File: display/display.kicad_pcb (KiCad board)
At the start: 2 copper layers, 68.4 x 20.5 mm, 46 parts, among them P1 CONN_14

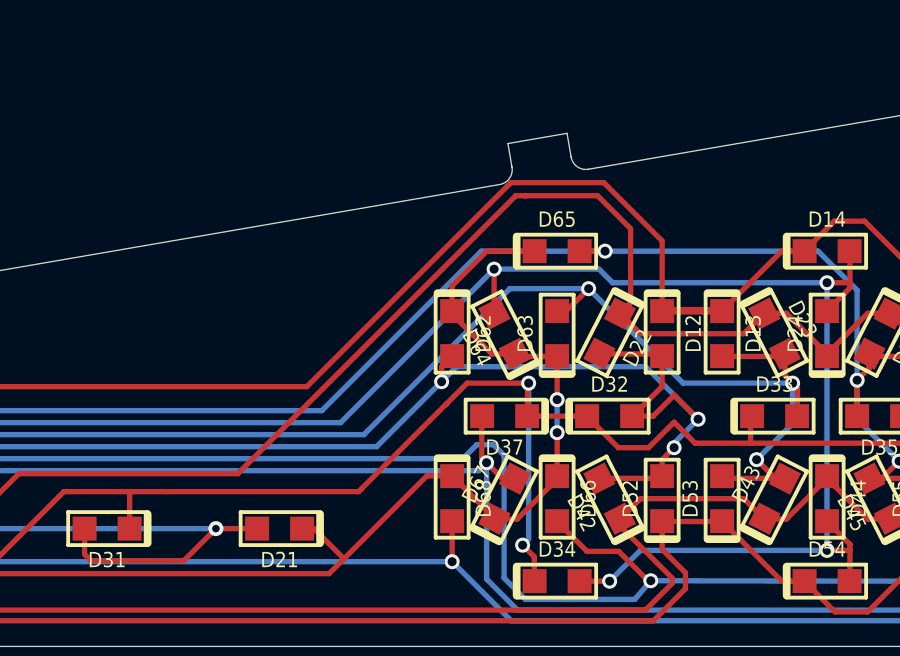
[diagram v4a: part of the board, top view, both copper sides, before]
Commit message: Route tracks farther from the contour.
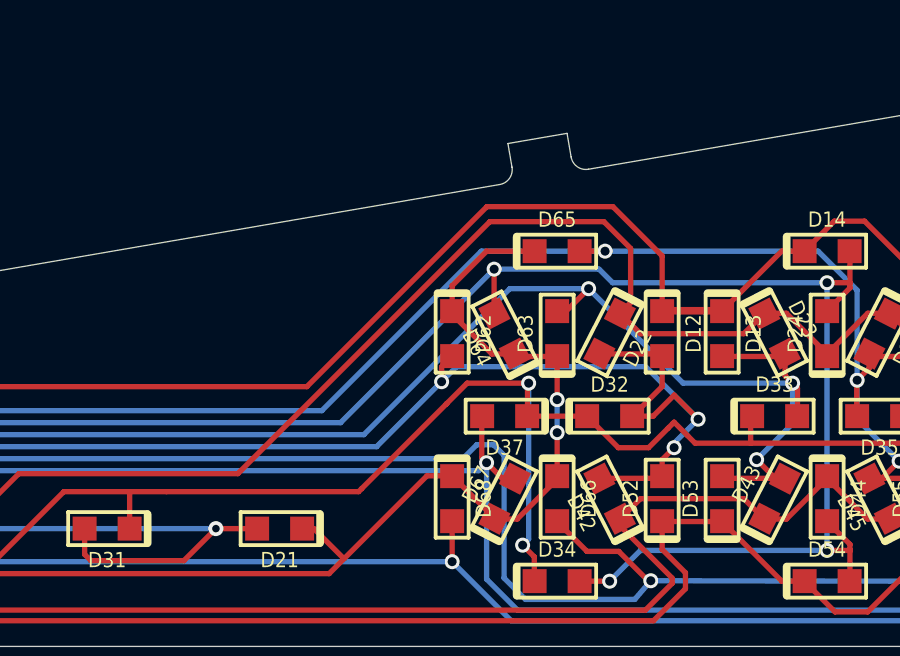
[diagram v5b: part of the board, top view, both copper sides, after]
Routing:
- net (no net): track 0.00 -> 57.8 mm
- net /ROW2: track 60.9 -> 18.8 mm
- net /ROW1: track 63.4 -> 45.6 mm
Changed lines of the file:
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@@
     (thickness 1.6002)
     (drawings 33)
-    (tracks 382)
+    (tracks 379)
     (zones 0)
     (modules 46)
@@
   (gr_line (start 135.992156 96.388669) (end 136.127883 97.177067) (angle 90) (layer Edge.Cuts) (width 0.01))
   (gr_arc (start 135.635143 97.2619) (end 135.719962 97.754651) (angle -90.01309679) (layer Edge.Cuts) (width 0.01))
+  (segment (start 160.84296 98.58178) (end 160.84296 96.74296) (width 0.1778) (layer Front) (net 0) (status 400000))
+  (segment (start 131.419099 101.1) (end 149 101.1) (width 0.1778) (layer Front) (net 9) (status 1000000))
+  (segment (start 131.419099 101.1) (end 130.402749 102.11635) (width 0.1778) (layer Front) (net 9) (status 1000000))
+  (segment (start 155 95.1) (end 149 101.1) (width 0.1778) (layer Front) (net 0) (status 1000000))
+  (segment (start 159.2 95.1) (end 155 95.1) (width 0.1778) (layer Front) (net 0) (status 1000000))
+  (segment (start 160.84296 96.74296) (end 159.2 95.1) (width 0.1778) (layer Front) (net 0) (status 1000000))
+  (segment (start 159.7914 98.30308) (end 159.7914 96.4914) (width 0.1778) (layer Front) (net 0))
+  (segment (start 146.7 104) (end 139.39936 104) (width 0.1778) (layer Front) (net 10))
+  (segment (start 139.39936 104) (end 137.56772 105.83164) (width 0.1778) (layer Front) (net 10))
+  (segment (start 174.01032 98.6536) (end 175.34128 99.98456) (width 0.1778) (layer Front) (net 0))
+  (segment (start 175.34128 99.98456) (end 175.34128 100.09378) (width 0.1778) (layer Front) (net 0))
+  (segment (start 175.34128 100.00742) (end 176.6951 98.6536) (width 0.1778) (layer Front) (net 0))
+  (segment (start 176.6951 98.6536) (end 177.43932 98.6536) (width 0.1778) (layer Front) (net 0))
+  (segment (start 175.34128 100.09378) (end 175.34128 100.00742) (width 0.1778) (layer Front) (net 0))
+  (segment (start 164.24402 98.6536) (end 163.5633 99.33432) (width 0.1778) (layer Front) (net 0))
+  (segment (start 160.1216 99.33432) (end 159.44088 98.6536) (width 0.1778) (layer Front) (net 0))
+  (segment (start 163.5633 99.33432) (end 160.1216 99.33432) (width 0.1778) (layer Front) (net 0))
+  (segment (start 166.34206 100.09378) (end 166.34206 100.00996) (width 0.1778) (layer Front) (net 0))
+  (segment (start 164.9857 98.6536) (end 164.24402 98.6536) (width 0.1778) (layer Front) (net 0))
+  (segment (start 166.34206 100.00996) (end 164.9857 98.6536) (width 0.1778) (layer Front) (net 0))
+  (segment (start 168.4401 98.6536) (end 167.69588 98.6536) (width 0.1778) (layer Front) (net 0))
+  (segment (start 166.34206 100.00742) (end 166.34206 100.09378) (width 0.1778) (layer Front) (net 0))
+  (segment (start 167.69588 98.6536) (end 166.34206 100.00742) (width 0.1778) (layer Front) (net 0))
+  (segment (start 173.24324 98.6536) (end 172.56252 99.33432) (width 0.1778) (layer Front) (net 0))
+  (segment (start 169.12082 99.33432) (end 168.4401 98.6536) (width 0.1778) (layer Front) (net 0))
+  (segment (start 172.56252 99.33432) (end 169.12082 99.33432) (width 0.1778) (layer Front) (net 0))
+  (segment (start 173.24324 98.6536) (end 174.01032 98.6536) (width 0.1778) (layer Front) (net 0))
+  (segment (start 159.44088 98.6536) (end 159.7914 98.30308) (width 0.1778) (layer Front) (net 0))
+  (segment (start 155.1 95.6) (end 146.7 104) (width 0.1778) (layer Front) (net 0))
+  (segment (start 158.9 95.6) (end 155.1 95.6) (width 0.1778) (layer Front) (net 0))
+  (segment (start 159.7914 96.4914) (end 158.9 95.6) (width 0.1778) (layer Front) (net 0))
   (segment (start 129.634 106.934) (end 128.266 106.934) (width 0.1778) (layer Back) (net 1))
   (via (at 128.2 107) (size 0.50038) (layers Front Back) (net 1))
@@
   (segment (start 141.59272 106.69272) (end 141.8 106.9) (width 0.1778) (layer Front) (net 2))
   (segment (start 141.59272 105.83164) (end 141.59272 106.69272) (width 0.1778) (layer Front) (net 2))
+  (segment (start 127 103.9) (end 154.72534 103.9) (width 0.1778) (layer Back) (net 3))
   (segment (start 126.8 104.1) (end 127 103.9) (width 0.1778) (layer Back) (net 3))
   (segment (start 126.892845 105.364911) (end 126.7 104.3) (width 0.1778) (layer Front) (net 3))
@@
   (segment (start 126.7 104.3) (end 126.8 104.1) (width 0.1778) (layer Front) (net 3))
   (segment (start 154.72534 103.9) (end 154.9908 103.63454) (width 0.1778) (layer Back) (net 3))
-  (segment (start 127 103.9) (end 154.72534 103.9) (width 0.1778) (layer Back) (net 3))
   (segment (start 175.34128 106.48442) (end 173.2788 108.5469) (width 0.1778) (layer Back) (net 3))
   (segment (start 154.9908 107.5182) (end 154.9908 103.63454) (width 0.1778) (layer Back) (net 3))
@@
   (segment (start 167.82796 100.09378) (end 167.74414 100.00996) (width 0.1778) (layer Front) (net 8))
   (segment (start 130.834477 104.684073) (end 130.402749 102.11635) (width 0.1778) (layer Front) (net 9))
-  (segment (start 160.84296 98.58178) (end 160.84296 96.24296) (width 0.1778) (layer Front) (net 9))
-  (segment (start 131.419099 101.1) (end 130.402749 102.11635) (width 0.1778) (layer Front) (net 9))
-  (segment (start 149 101.1) (end 155.8 94.3) (width 0.1778) (layer Front) (net 9))
-  (segment (start 131.419099 101.1) (end 149 101.1) (width 0.1778) (layer Front) (net 9))
-  (segment (start 160.84296 96.24296) (end 158.9 94.3) (width 0.1778) (layer Front) (net 9))
-  (segment (start 158.9 94.3) (end 155.8 94.3) (width 0.1778) (layer Front) (net 9))
   (segment (start 169.84218 98.56978) (end 169.84218 97.83572) (width 0.1778) (layer Front) (net 9))
   (segment (start 166.58082 95.58274) (end 165.58006 96.5835) (width 0.1778) (layer Front) (net 9))
@@
   (segment (start 130.6 106.2) (end 130.341773 104.769178) (width 0.1778) (layer Front) (net 10))
   (segment (start 131 106.6) (end 136.79936 106.6) (width 0.1778) (layer Front) (net 10))
-  (segment (start 146.8 103.9) (end 146.7 104) (width 0.1778) (layer Front) (net 10))
-  (segment (start 156.3 94.73438) (end 155.96562 94.73438) (width 0.1778) (layer Front) (net 10))
-  (segment (start 155.96562 94.73438) (end 146.8 103.9) (width 0.1778) (layer Front) (net 10))
-  (segment (start 139.39936 104) (end 137.56772 105.83164) (width 0.1778) (layer Front) (net 10))
-  (segment (start 146.7 104) (end 139.39936 104) (width 0.1778) (layer Front) (net 10))
-  (segment (start 159.44088 98.6536) (end 159.7914 98.30308) (width 0.1778) (layer Front) (net 10))
-  (segment (start 173.24324 98.6536) (end 174.01032 98.6536) (width 0.1778) (layer Front) (net 10))
-  (segment (start 172.56252 99.33432) (end 169.12082 99.33432) (width 0.1778) (layer Front) (net 10))
-  (segment (start 169.12082 99.33432) (end 168.4401 98.6536) (width 0.1778) (layer Front) (net 10))
-  (segment (start 173.24324 98.6536) (end 172.56252 99.33432) (width 0.1778) (layer Front) (net 10))
-  (segment (start 167.69588 98.6536) (end 166.34206 100.00742) (width 0.1778) (layer Front) (net 10))
-  (segment (start 166.34206 100.00742) (end 166.34206 100.09378) (width 0.1778) (layer Front) (net 10))
-  (segment (start 168.4401 98.6536) (end 167.69588 98.6536) (width 0.1778) (layer Front) (net 10))
-  (segment (start 166.34206 100.00996) (end 164.9857 98.6536) (width 0.1778) (layer Front) (net 10))
-  (segment (start 164.9857 98.6536) (end 164.24402 98.6536) (width 0.1778) (layer Front) (net 10))
-  (segment (start 166.34206 100.09378) (end 166.34206 100.00996) (width 0.1778) (layer Front) (net 10))
-  (segment (start 163.5633 99.33432) (end 160.1216 99.33432) (width 0.1778) (layer Front) (net 10))
-  (segment (start 160.1216 99.33432) (end 159.44088 98.6536) (width 0.1778) (layer Front) (net 10))
-  (segment (start 164.24402 98.6536) (end 163.5633 99.33432) (width 0.1778) (layer Front) (net 10))
-  (segment (start 159.7914 98.30308) (end 159.7914 95.8342) (width 0.1778) (layer Front) (net 10))
-  (segment (start 159.7914 95.8342) (end 158.69158 94.73438) (width 0.1778) (layer Front) (net 10))
-  (segment (start 158.69158 94.73438) (end 156.3 94.73438) (width 0.1778) (layer Front) (net 10))
-  (segment (start 156.3 94.73438) (end 156.24048 94.73438) (width 0.1778) (layer Front) (net 10))
-  (segment (start 175.34128 100.09378) (end 175.34128 100.00742) (width 0.1778) (layer Front) (net 10))
-  (segment (start 176.6951 98.6536) (end 177.43932 98.6536) (width 0.1778) (layer Front) (net 10))
-  (segment (start 175.34128 100.00742) (end 176.6951 98.6536) (width 0.1778) (layer Front) (net 10))
-  (segment (start 175.34128 99.98456) (end 175.34128 100.09378) (width 0.1778) (layer Front) (net 10))
-  (segment (start 174.01032 98.6536) (end 175.34128 99.98456) (width 0.1778) (layer Front) (net 10))
   (segment (start 143.09272 105.83164) (end 143.09272 104.6) (width 0.1778) (layer Front) (net 11))
   (segment (start 143.09272 104.6) (end 143.1 104.6) (width 0.1778) (layer Front) (net 11))
